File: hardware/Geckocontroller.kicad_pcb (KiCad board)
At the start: 2 copper layers, 114.3 x 96.5 mm, 113 parts, among them J101 AC Input, J11 RGB LED, J21 I²C (BME280), J31 DS18B20 I, J32 DS18B20 II, J40 FAN, J50 USB-C, J51 UART, J60 Load Cell Connector, J70 SPI / Addon Connector, J81 Dimmer, J91 Pump, J92 HeatBed, J93 HeatLamp, K81 AQG12212, K91 AQG12112, K92 AQG12112, K93 AQG12112, Q11 AO3400A, Q12 AO3400A, Q13 AO3400A, Q40 AO3400A, Q41 AO3401A, Q51 S8050, Q52 S8050, Q61 S8550, Q81 AO3400A, Q91 AO3400A, Q92 AO3400A, Q93 AO3400A, SW1 Boot, SW2 Reset, U1 ESP32-WROOM-32, U101 ACT4088, U2 CP2102, U61 HX711, U81 6N138

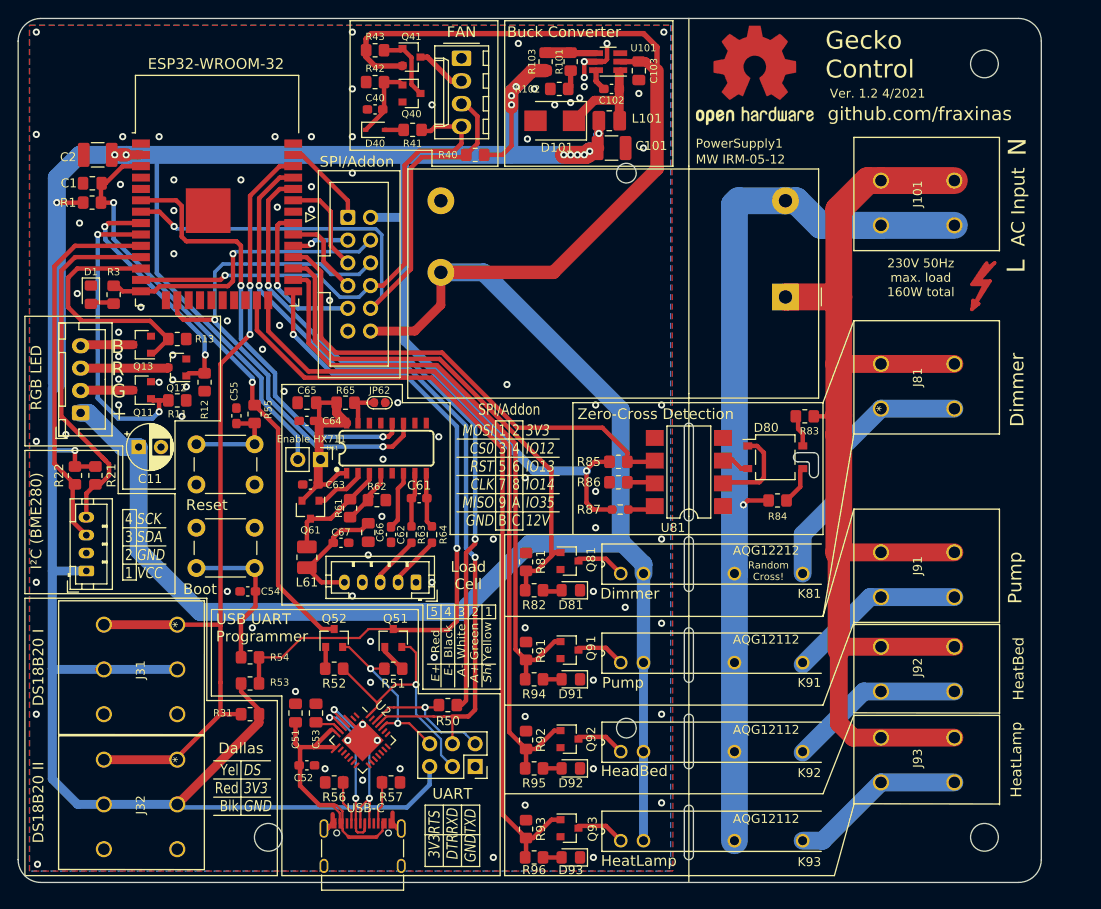
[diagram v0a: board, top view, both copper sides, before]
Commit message: PCB: Move around modules and masks a little more
No functional changes
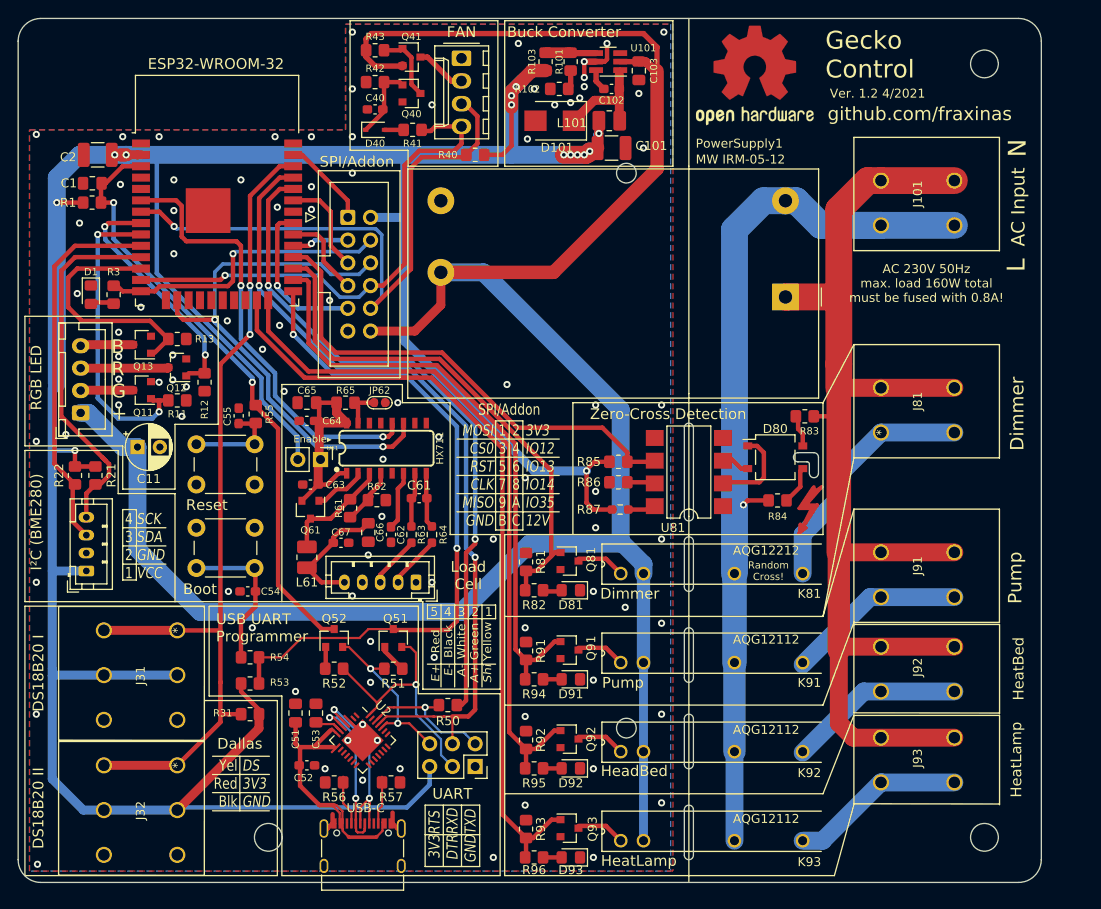
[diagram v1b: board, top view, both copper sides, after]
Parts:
- moved REF** 31.6 mm to (102.9, 68.2)
- moved J81 2.67 mm to (111.6, 59.0)
- moved J31 0.63 mm to (33.0, 81.1)
- moved J32 0.63 mm to (33.0, 96.1)
- moved C55 0.25 mm to (39.9, 57.1)
- moved C11 0.13 mm to (28.6, 60.6)
- moved R55 0.13 mm to (41.8, 56.9)
- turned L101 to 0 degrees
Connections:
- L101 pad 1: Net-(C102-Pad1) -> +3V3
- L101 pad 2: +3V3 -> Net-(C102-Pad1)
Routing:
- net /L_Dimmer: track 30.2 -> 27.6 mm
- net /L: track 103.0 -> 101.4 mm
- net /DS_in: track 97.0 -> 97.5 mm
- net GND: vias 93 -> 92
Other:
- board text added: "AC 230V 50Hz max. load 160W total must be fused with 0.8A!"
- board text added: "Enable▸"
- board text removed: "230V 50Hz max. load 160W total"

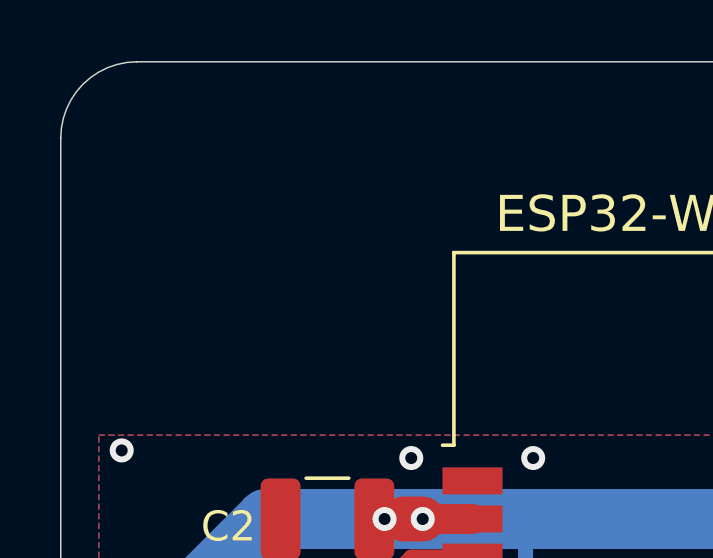
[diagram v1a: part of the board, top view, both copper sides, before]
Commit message: PCB: Add Smol Gecko Footprint, add silkscreen logos
Commissioned for production with Aisler on 2021-04-15
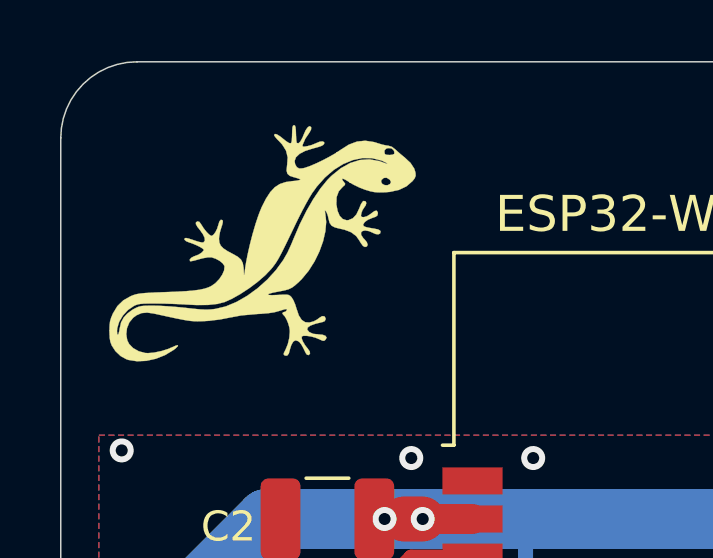
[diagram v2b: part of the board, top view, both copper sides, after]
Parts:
- added G***: LOGO, Fraxinas:gecko_smol, F.Cu at (26.9, 22.6)
- added G***: LOGO, Fraxinas:repairfox, F.Cu at (52.1, 72.8)
- added G***: LOGO, Fraxinas:purplegecko, F.Cu at (37.5, 28.2)
